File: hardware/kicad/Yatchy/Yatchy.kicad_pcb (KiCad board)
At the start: 4 copper layers, 33.8 x 46 mm, 94 parts, among them IC2 MCP23018-E_MJ, IC3 MCP73831T-2ATI_OT, J1 MOD_CONN, J10 MOD_CONN, J11 MOD_CONN, J12 MOD_CONN, J13 MOD_CONN, J14 MOD_CONN, J15 MOD_CONN, J16 MOD_CONN, J19 MOD_CONN, J2 MOD_CONN, J20 MOD_CONN, J21 MOD_CONN, J22 MOD_CONN, J23 MOD_CONN, J24 MOD_CONN, J25 MOD_CONN, J26 Conn_01x03_Pin, J27 MOD_CONN, J28 Conn_01x02_Pin, J3 MOD_CONN, J4 USB4730-GF-A-KIT, J5 SFV24R-4STBE1HLF, J6 MOD_CONN, J7 MOD_CONN, J8 MOD_CONN, J9 MOD_CONN, M1 Vibration_Motor, Q1 AO3400A, Q4 FDN304PZ, Q5 S8050, SW1 EVP-AKE31A, SW2 EVP-AKE31A, SW3 EVP-AKE31A, U1 USBLC6-2P6, U2 TLV75533PDBV, U3 ESP32-C6-MINI-1-N4, Y2 32.768KHz

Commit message: change motor transistor name
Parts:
- Q5: value S8050 -> BC817-25.215
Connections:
- net MOD_RX renamed RX
- net MOD_TX renamed TX

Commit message: change tvs diode fix module and calc
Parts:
- removed R12: 10K, Resistor_SMD:R_0402_1005Metric
- removed U1: USBLC6-2P6, Yatchy:SOT-666
- added D1: D_TVS, Diode_SMD:D_SOD-523, F.Cu at (88.8, 97.6)
- added D3: D_TVS, Diode_SMD:D_SOD-523, F.Cu at (88.8, 96.2)
- added D4: D_TVS, Diode_SMD:D_SOD-523, F.Cu at (91.5, 96.6)
- moved R13 0.51 mm to (89.6, 99.0)
- moved C2 0.44 mm to (87.0, 99.1)
- moved C21 0.34 mm to (91.5, 99.2)
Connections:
- IC2 pad 12: Net-(IC2-~{RESET}) -> +3V3
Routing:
- net GND: track 187.7 -> 196.3 mm
- net +3V3: track 133.0 -> 136.3 mm
- net Net-(IC2-~{RESET}): track 2.25 -> 0.00 mm
- net VBUS: track 81.6 -> 80.1 mm

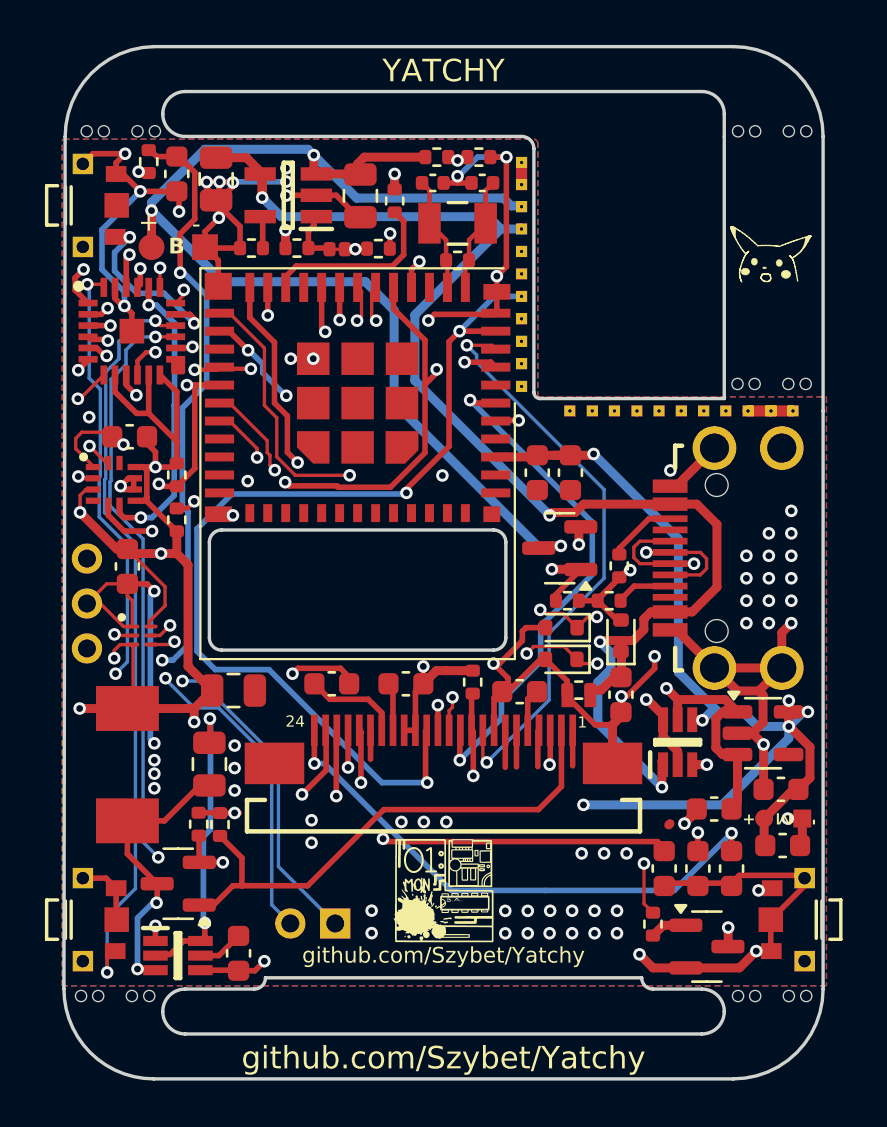
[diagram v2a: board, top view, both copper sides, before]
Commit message: remove mouse bites
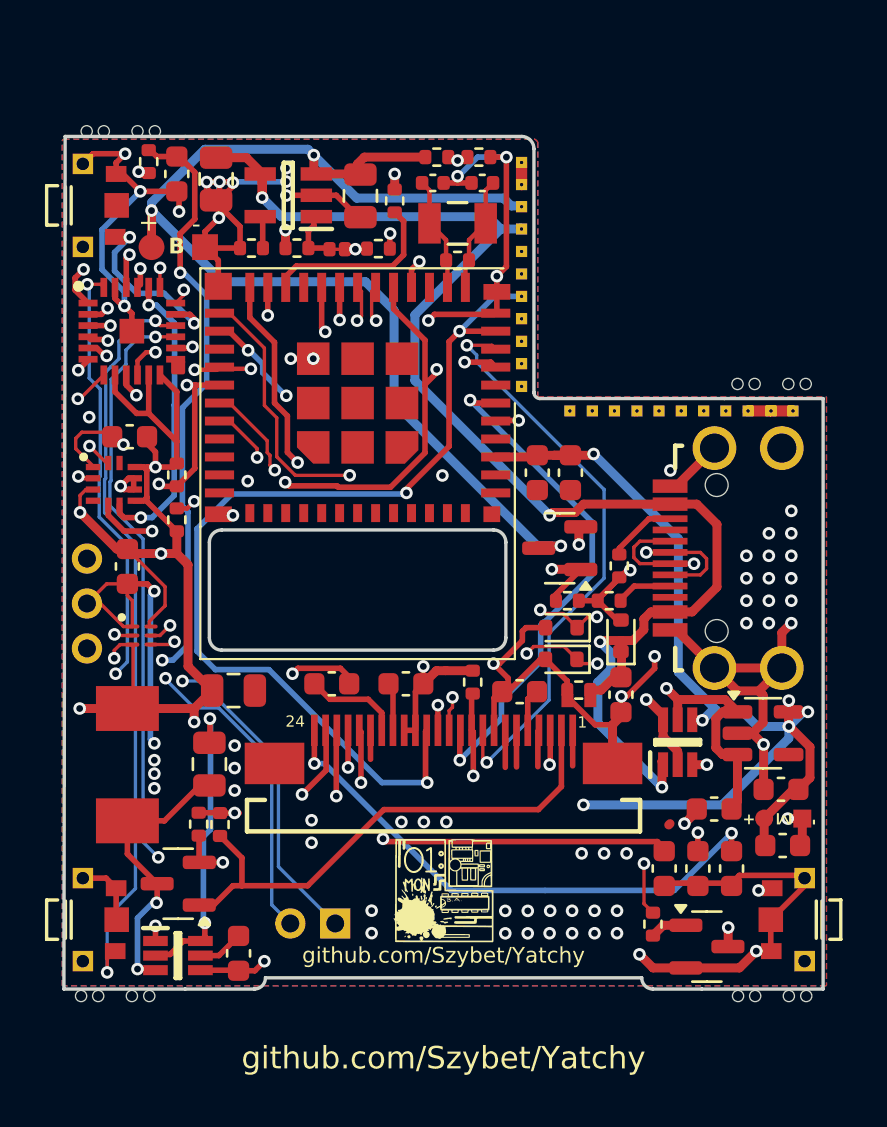
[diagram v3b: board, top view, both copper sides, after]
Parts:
- removed the G*** at (98.6, 79.7)
- removed U4: ~, Yatchy:mouse-bite-3mm-slot
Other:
- board size 33.8 x 46 mm -> 33.8 x 38 mm
- board text removed: "YATCHY"

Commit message: fix outline
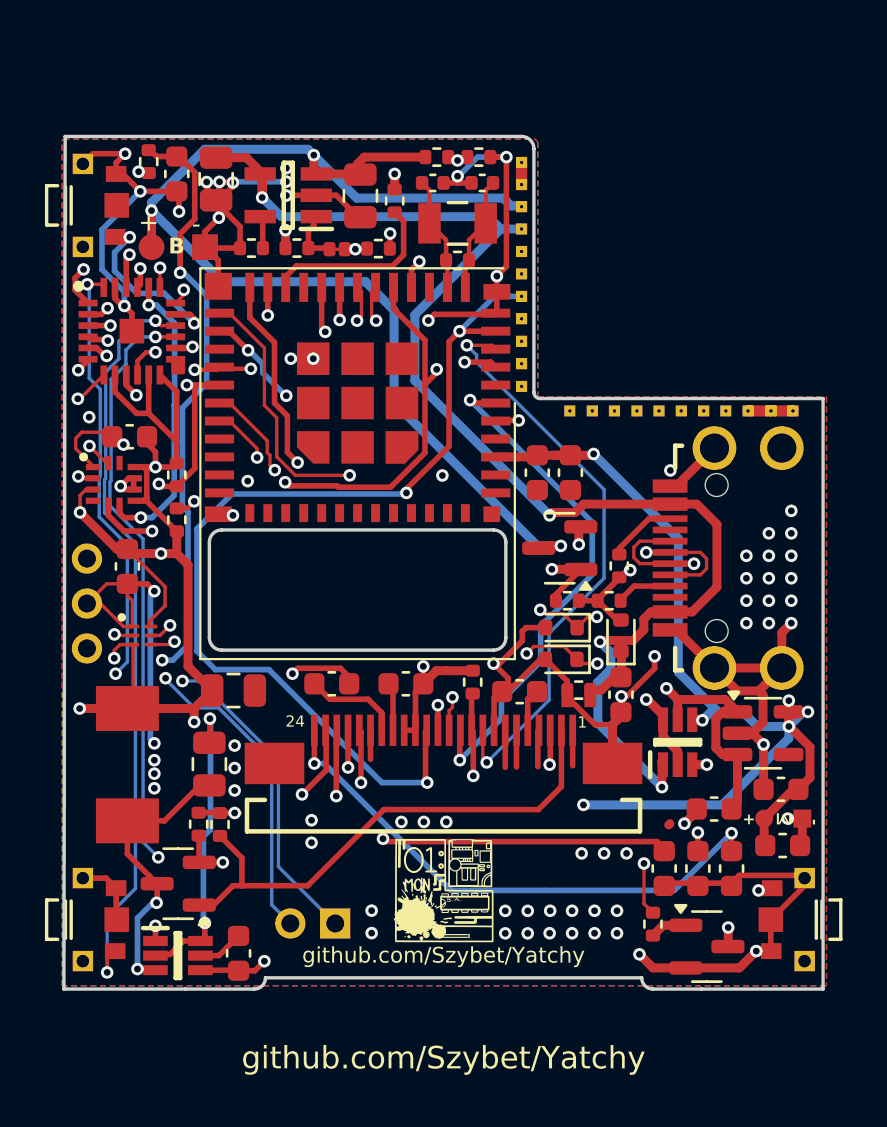
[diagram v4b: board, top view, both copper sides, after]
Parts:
- removed U5, U6, U7, U8: ~, Yatchy:mouse-bite-3mm-slot
- R1, R2: value 5.1k -> 100k

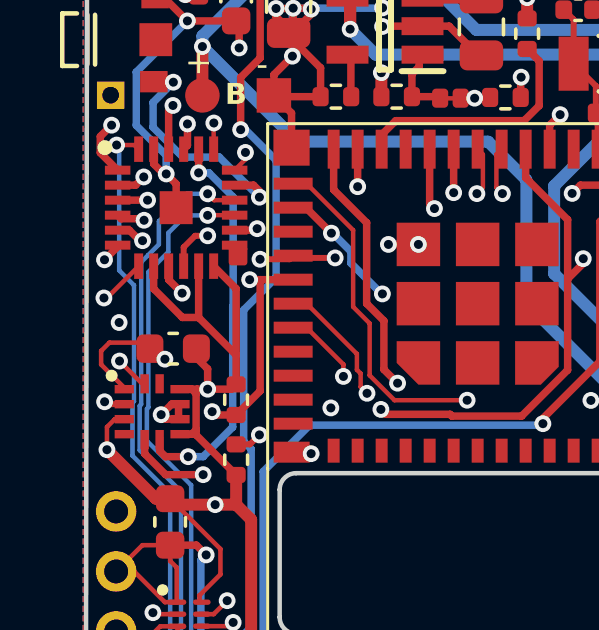
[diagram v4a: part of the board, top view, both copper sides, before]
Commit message: fix components-calc based on bom file, add 1K resistor to gpio expander 5V connection, change 50K resistor to 100K
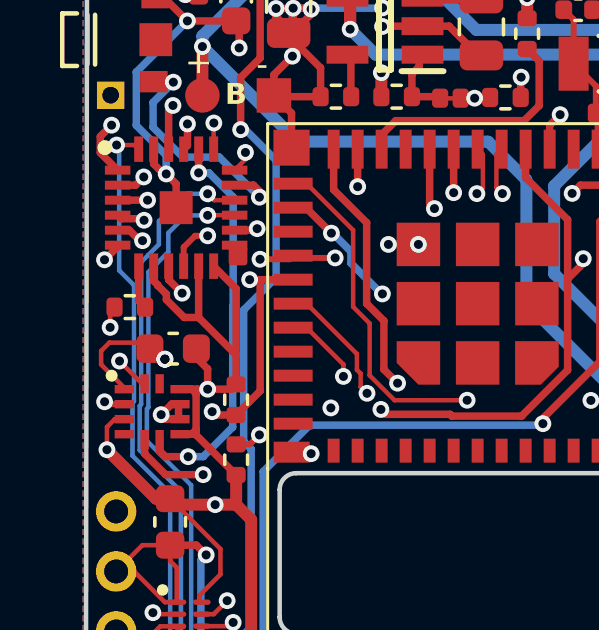
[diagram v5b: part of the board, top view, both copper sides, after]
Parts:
- added R19: 1K, Resistor_SMD:R_0402_1005Metric, F.Cu at (68.2, 86.3)
- R13: value 50k -> 100K
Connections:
- IC2 pad 7: VBUS -> Net-(IC2-GPB7)
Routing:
- net Net-(IC2-GPB7): track 0.00 -> 1.45 mm
- net GND: track 196.3 -> 197.1 mm

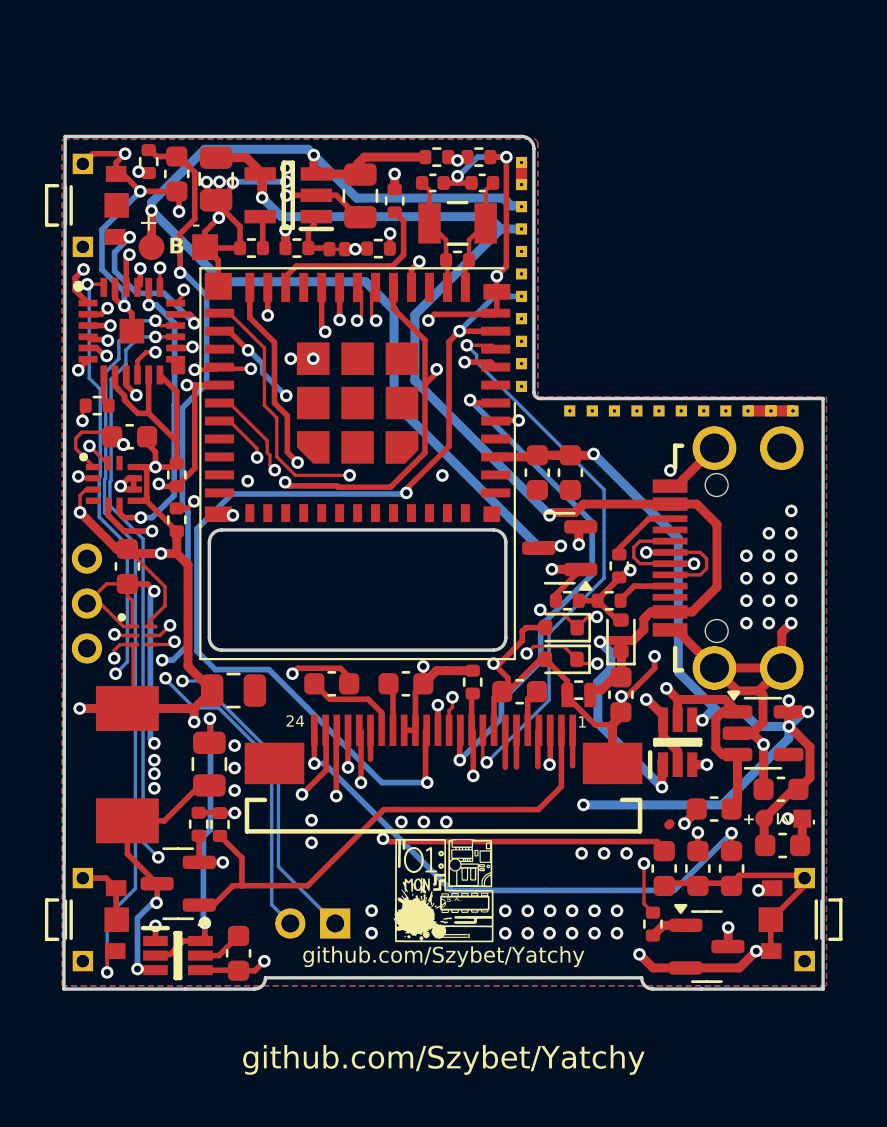
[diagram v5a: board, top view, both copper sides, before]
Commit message: connect mcp reset pin with esp32c6
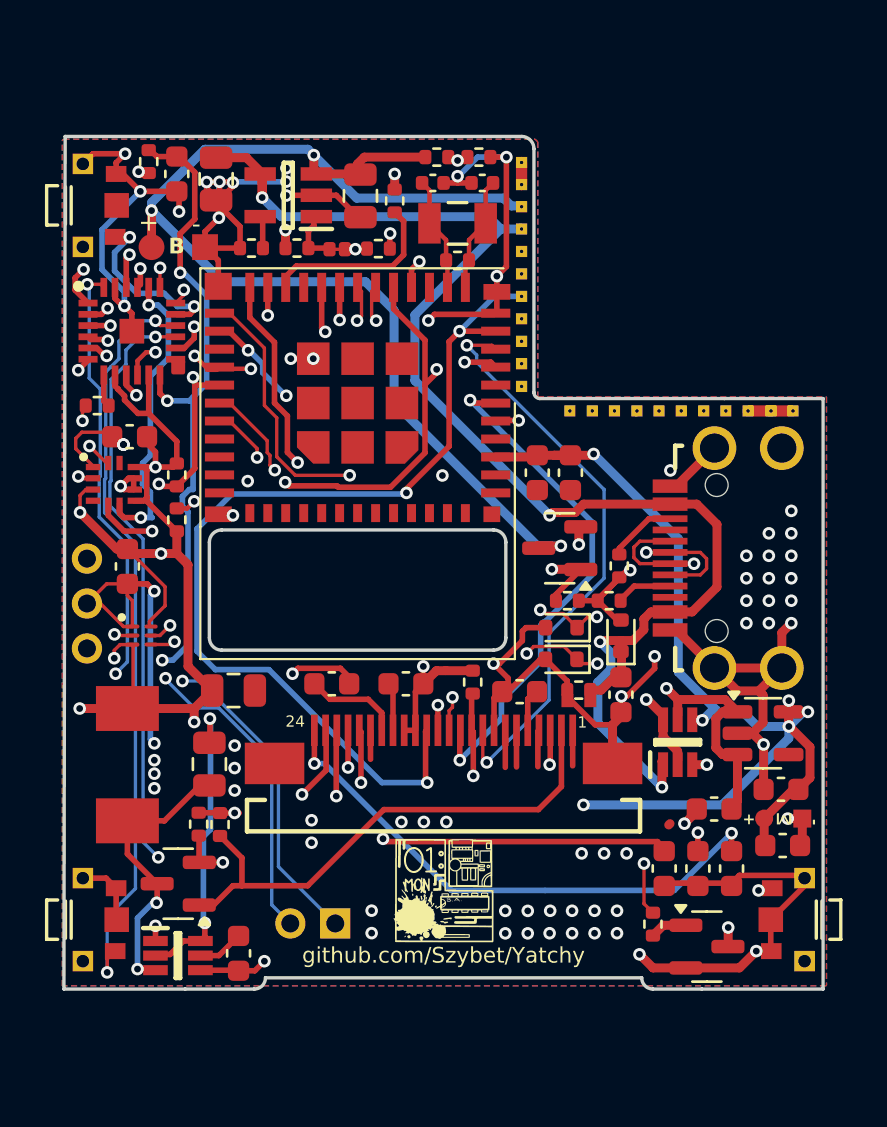
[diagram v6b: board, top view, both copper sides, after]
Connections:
- IC2 pad 12: +3V3 -> EN
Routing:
- net SCL: track 43.1 -> 46.9 mm
- net +3V3: track 136.3 -> 133.0 mm
- net EN: track 47.1 -> 49.7 mm, vias 3 -> 4
- net SDA: track 44.0 -> 44.7 mm
- net MOD_CS: track 27.4 -> 26.6 mm

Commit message: Some quality of life improvements to the pcb,  applied suggestions to the pcb
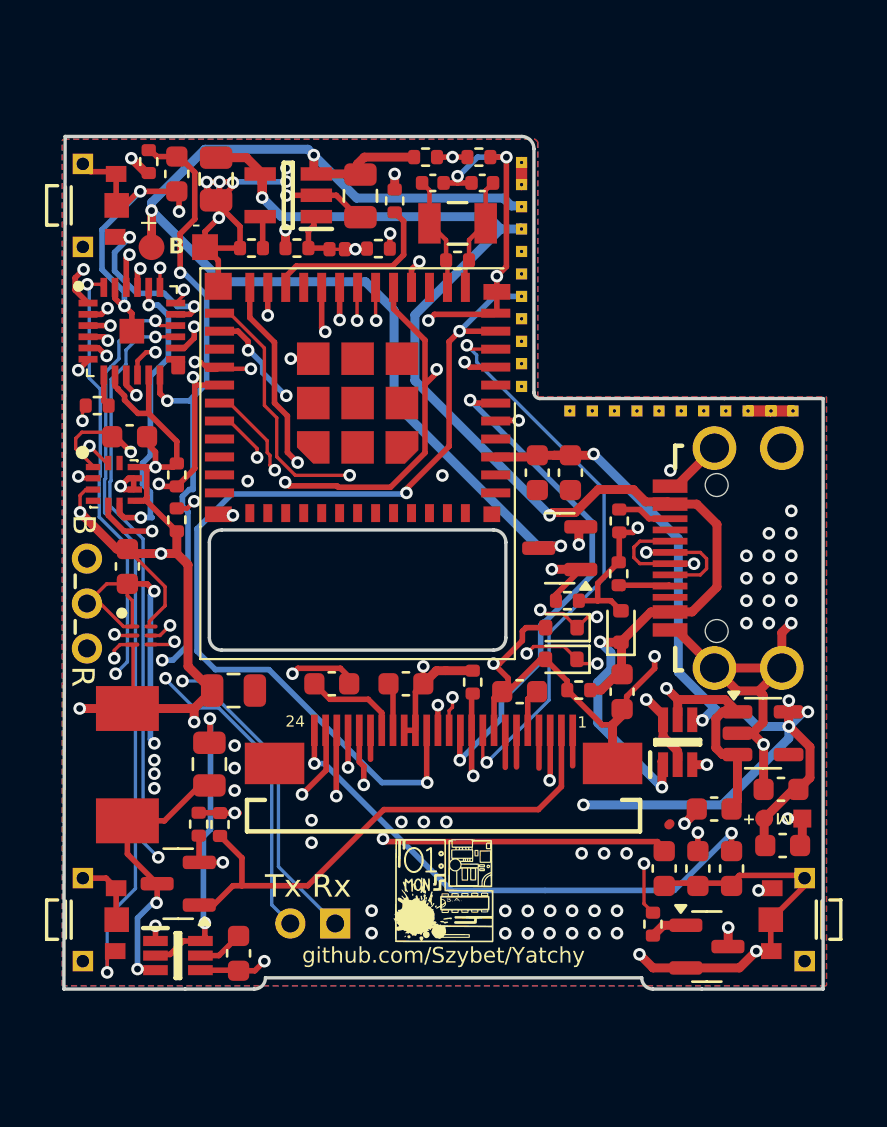
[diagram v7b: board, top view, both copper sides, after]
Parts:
- moved R4 2.00 mm to (91.4, 91.5)
- moved C23 1.47 mm to (87.8, 89.3)
- moved C24 1.47 mm to (89.2, 89.3)
- moved R5 1.27 mm to (91.4, 93.8), turned to 90 degrees
- moved R11 0.50 mm to (82.8, 75.3)
- moved D4 0.41 mm to (91.5, 96.2)
- moved C21 0.14 mm to (91.5, 99.1)
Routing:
- net GND: track 197.1 -> 203.1 mm, vias 77 -> 73
- net ADC: track 19.4 -> 20.8 mm
- net Net-(J4-CC2): track 3.08 -> 2.43 mm
- net +3V3: track 133.0 -> 133.6 mm
- net +BATT: track 54.9 -> 54.4 mm
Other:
- board text added: "B"
- board text added: "R"
- board text added: "Tx Rx"
